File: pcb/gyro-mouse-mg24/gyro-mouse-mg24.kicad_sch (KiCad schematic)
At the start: 10 parts, among them SW1 SW_SPST, U1 XIAO-MG24-SMD, U2 MPR121QR2

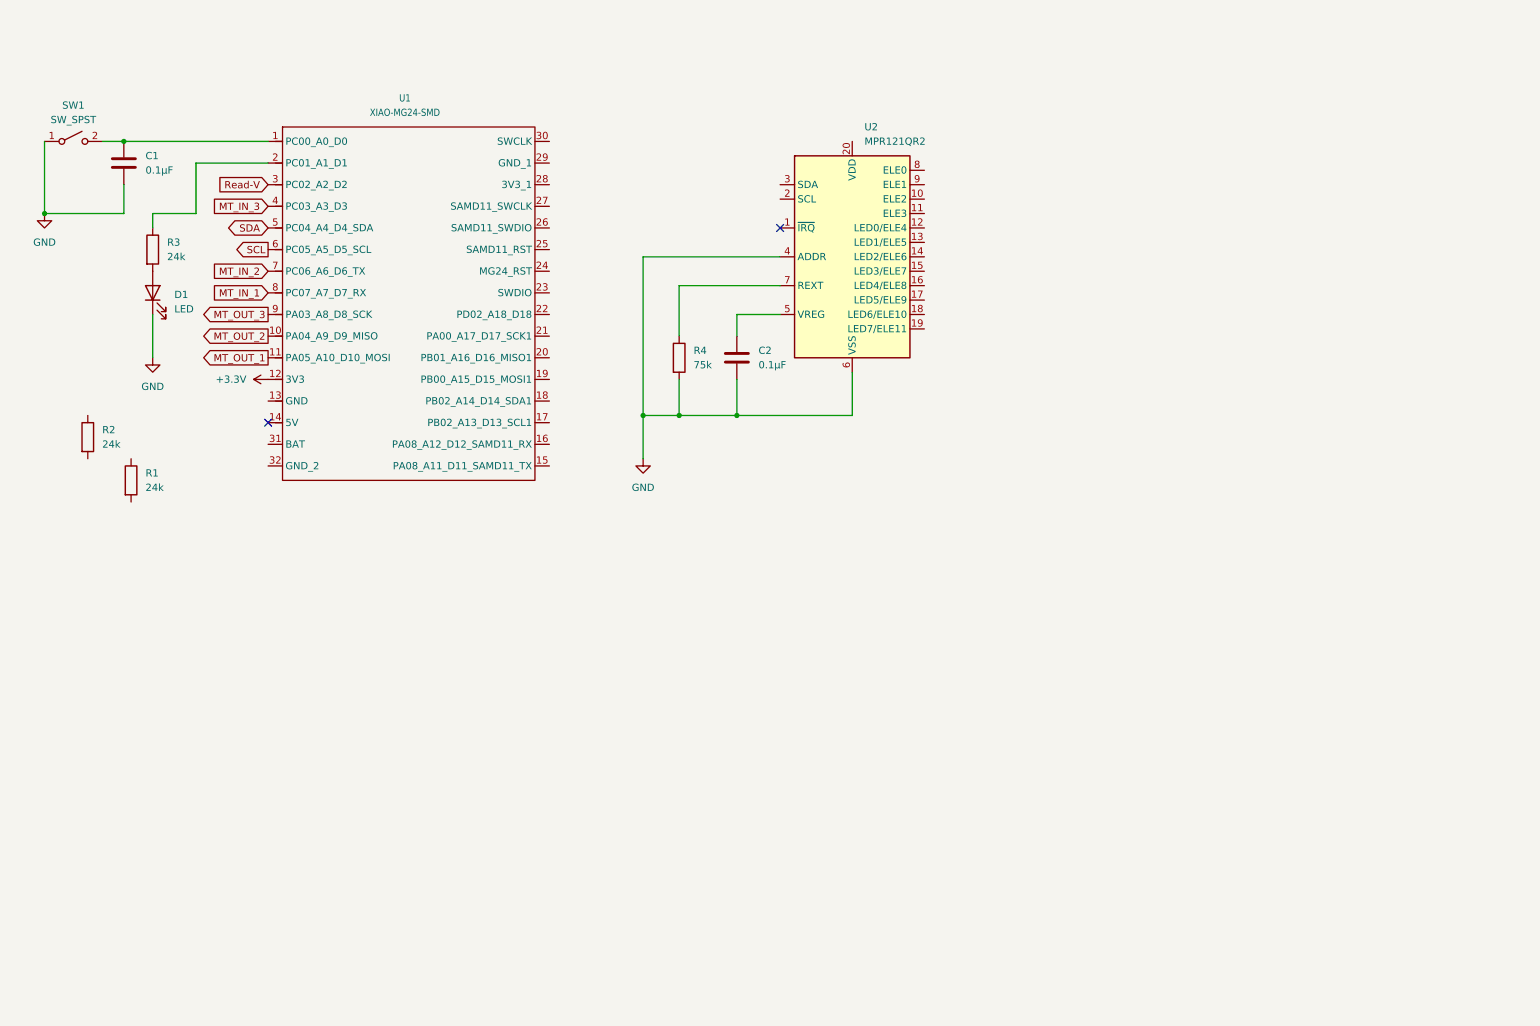
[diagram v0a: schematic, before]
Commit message: スイッチのマトリックス追加した
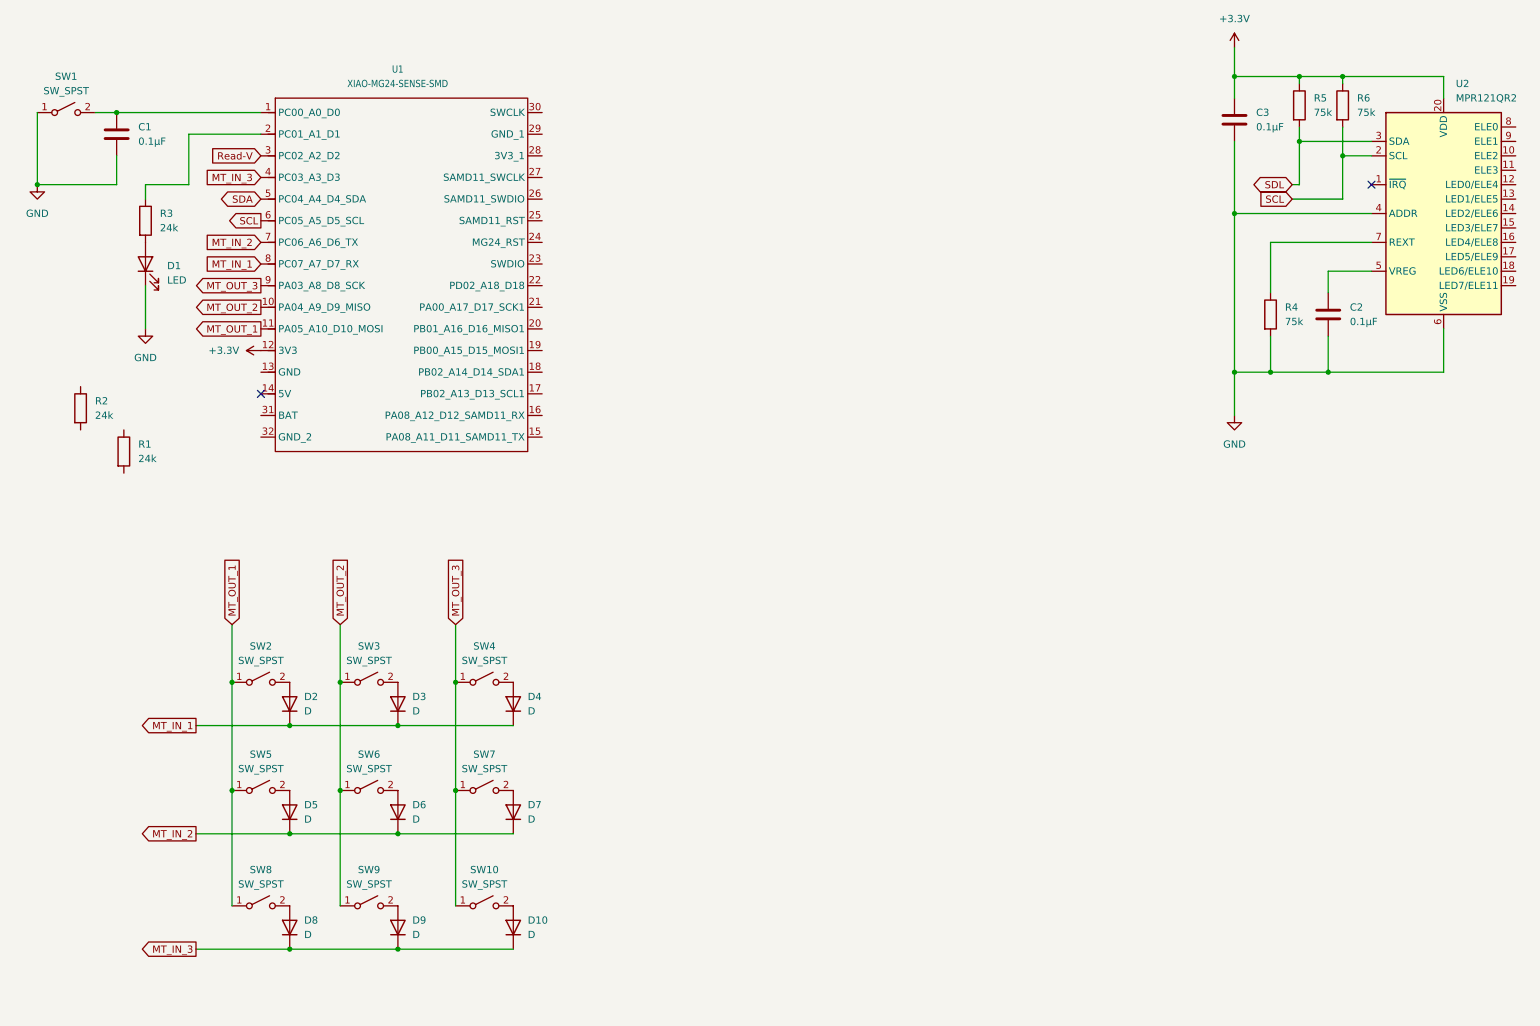
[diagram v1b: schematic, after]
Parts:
- added C3: 0.1μF, symbol Device:C
- added D10, D2, D3, D4, D5, D6, D7, D8, D9: D, symbol Device:D
- added R5, R6: 75k, symbol Device:R
- added SW10, SW2, SW3, SW4, SW5, SW6, SW7, SW8, SW9: SW_SPST, symbol Switch:SW_SPST
- U1: value XIAO-MG24-SMD -> XIAO-MG24-SENSE-SMD
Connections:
- net +3.3V: now also U2.20 (VDD), C3.1, R5.1, R6.1
- net GND: now also C3.2
- net MT_IN_1: now also D2.1 (K), D3.1 (K), D4.1 (K)
- net MT_IN_2: now also D5.1 (K), D6.1 (K), D7.1 (K)
- net MT_IN_3: now also D10.1 (K), D8.1 (K), D9.1 (K)
- net MT_OUT_1: now also SW2.1 (A), SW5.1 (A), SW8.1 (A)
- net MT_OUT_2: now also SW3.1 (A), SW6.1 (A), SW9.1 (A)
- net MT_OUT_3: now also SW10.1 (A), SW4.1 (A), SW7.1 (A)
- net SCL: now also U2.2 (SCL), R6.2
- net SDL: now reaches U2.3 (SDA)
- net SDL: now also R5.2
- new net: D8.2 (A), SW8.2 (B)
- new net: D4.2 (A), SW4.2 (B)
- new net: D5.2 (A), SW5.2 (B)
- new net: D6.2 (A), SW6.2 (B)
- new net: D2.2 (A), SW2.2 (B)
- new net: D7.2 (A), SW7.2 (B)
- new net: D9.2 (A), SW9.2 (B)
- new net: D10.2 (A), SW10.2 (B)
- new net: D3.2 (A), SW3.2 (B)
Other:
- moved on the sheet: C1, C2, D1, R1, R2, R3, R4, SW1, U1, U2

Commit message: バッテリー追加した
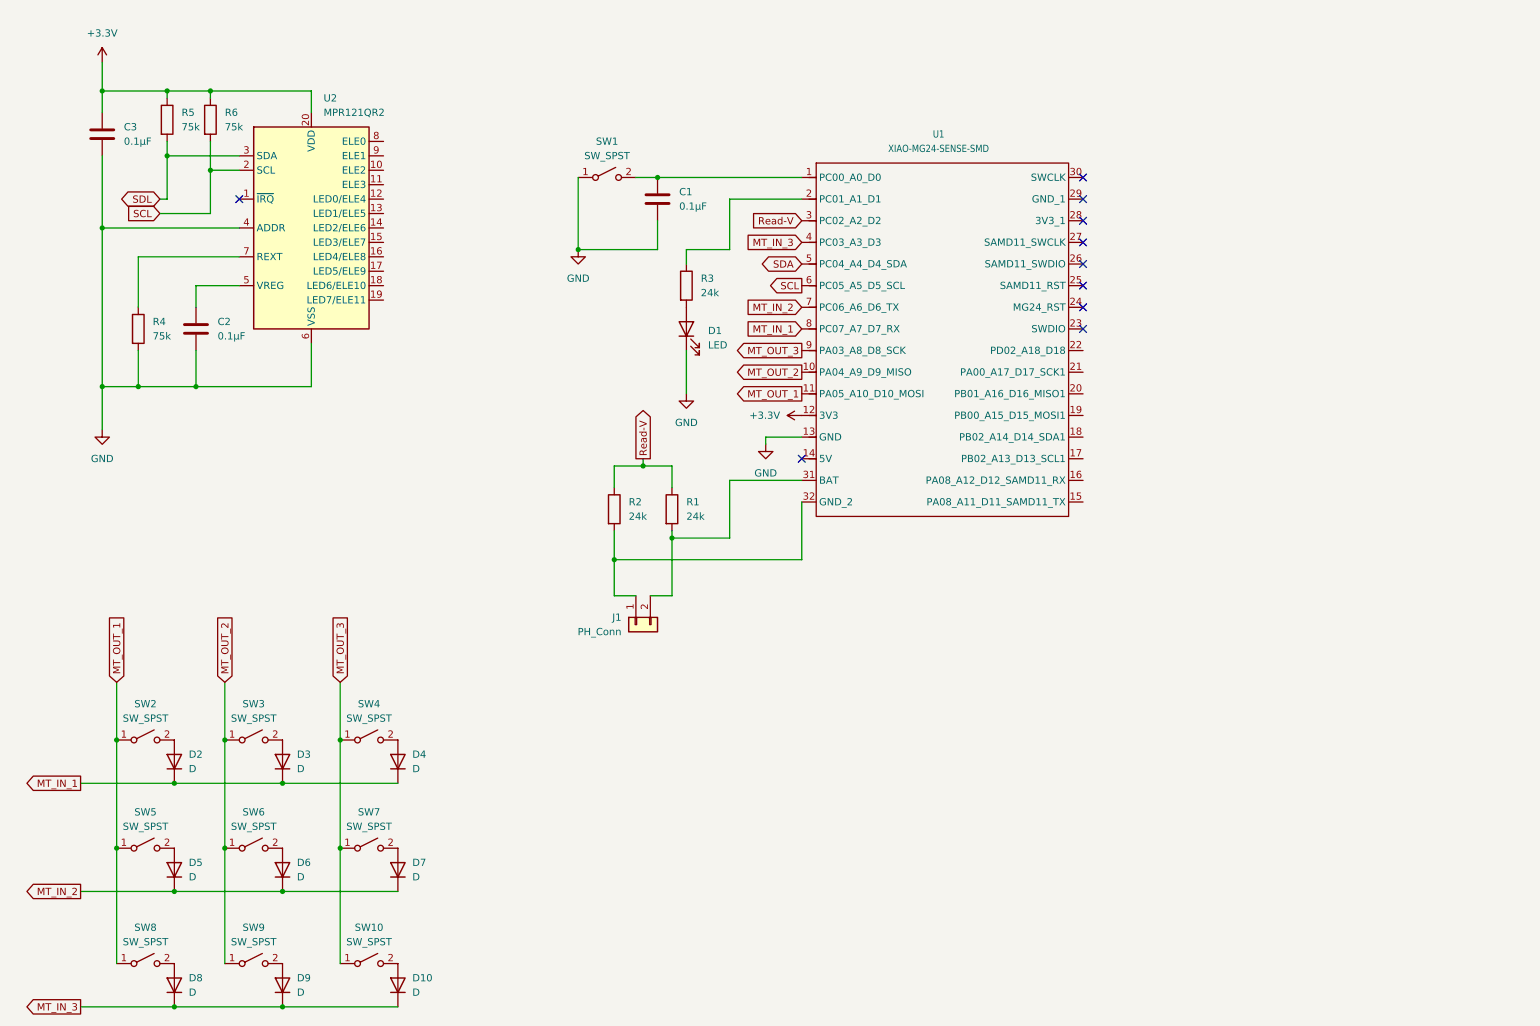
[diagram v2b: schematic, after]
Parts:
- added J1: PH_Conn, Connector_JST:JST_PH_S2B-PH-K_1x02_P2.00mm_Horizontal, symbol Connector_Generic:Conn_01x02
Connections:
- net GND: now also U1.13 (GND)
- net Read-V: now also R1.1, R2.1
- net at R1.2: now also U1.31 (BAT), J1.2 (Pin_2)
- net at U1.32 (GND_2): now also R2.2, J1.1 (Pin_1)
- no-connect marks 2 -> 10
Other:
- moved on the sheet: C1, C2, C3, D1, D10, D2, D3, D4, D5, D6, D7, D8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

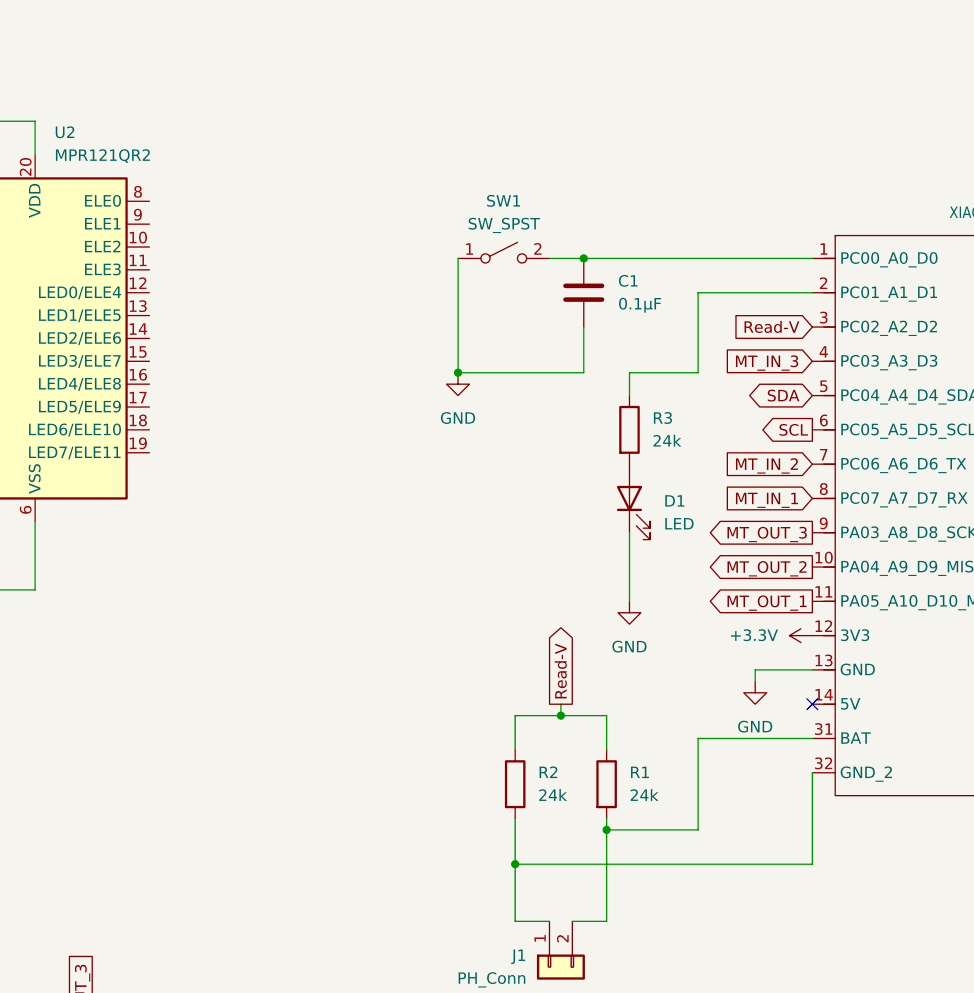
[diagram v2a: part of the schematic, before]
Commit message: ボタンに外部プルアップ抵抗を付けた
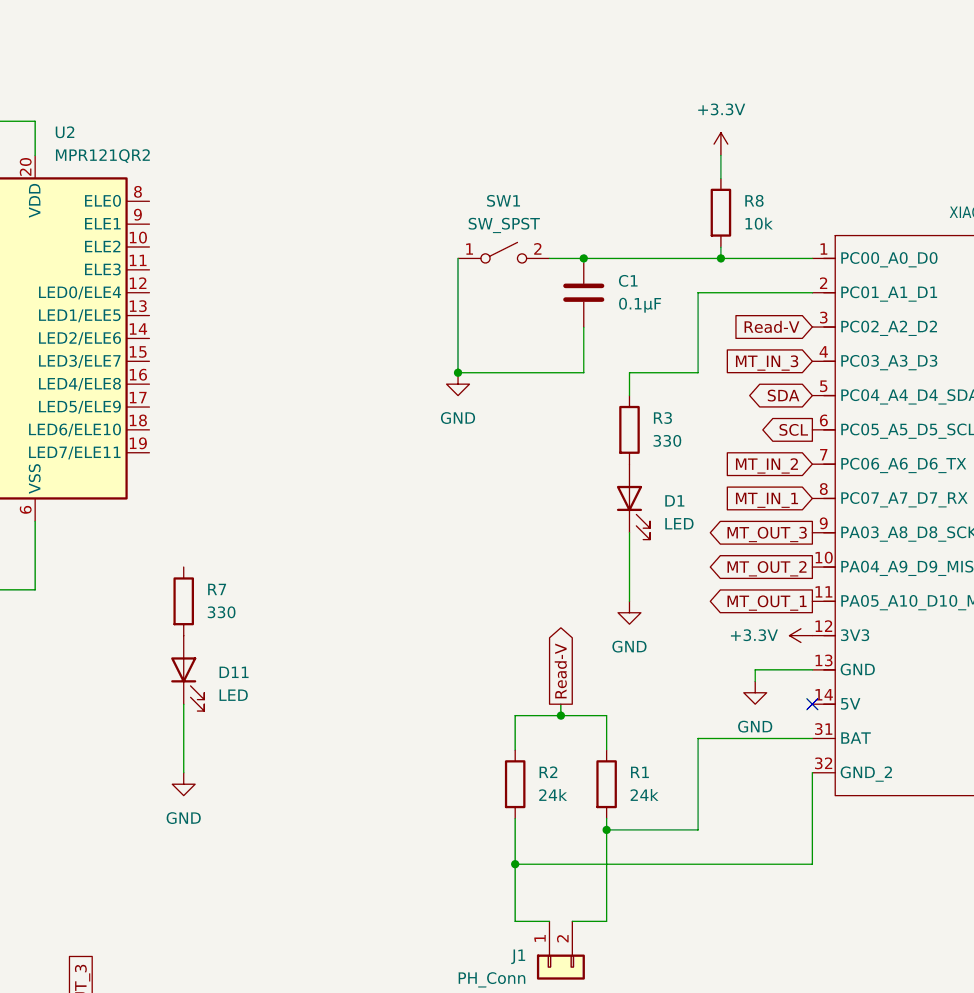
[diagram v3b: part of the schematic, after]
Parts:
- added D11: LED, symbol Device:LED
- added R7: 330, symbol Device:R
- added R8: 10k, symbol Device:R
- R3: value 24k -> 330
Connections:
- net +3.3V: now also R8.1
- net GND: now also D11.1 (K)
- net at C1.1, SW1.2 (B), U1.1 (PC00_A0_D0): now also R8.2
- new net: D11.2 (A), R7.2

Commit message: 回路図はいまのところこれでいく
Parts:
- R5, R6: value 75k -> 4.7k
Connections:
- net at R7.1: now also U2.1 (~{IRQ})
- no-connect marks 10 -> 9
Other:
- moved on the sheet: D11, R4, R5, R7
